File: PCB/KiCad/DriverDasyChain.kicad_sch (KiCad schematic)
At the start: 34 parts, among them J1 Conn_01x02, J10 Conn_01x06, J11 Conn_01x07_Socket, J12 Conn_01x03, J13 Conn_01x03, J16 Conn_01x02, J2 Conn_01x02, J4 Conn_01x04, J5 Conn_01x03, J7 Conn_01x07_Pin, J8 Conn_01x07_Pin, J9 Conn_01x07_Socket, Q2 Q_NMOS_GDS, SW2 SW_DPST_x2, U1 AP2112K-3.3, U2 XIAO-ESP32-S3-DIP, U3 74AHCT1G125, U4 SN65HVD230

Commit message: Keine Änderungen vorgenommen.
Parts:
- removed J1, J2: Conn_01x02, Connector_Molex:Molex_Micro-Fit_3.0_43650-0300_1x03_P3.00mm_Horizontal, symbol Connector_Generic:Conn_01x02
- removed J10: Conn_01x06, Connector_JST:JST_XH_B6B-XH-A_1x06_P2.50mm_Vertical, symbol Connector_Generic:Conn_01x06
- added C11: 100n, symbol Device:C
- added D2: D_Zener, symbol Device:D_Zener
- added J1, J2: Conn_01x03, Connector_Molex:Molex_Micro-Fit_3.0_43650-0300_1x03_P3.00mm_Horizontal, symbol Connector_Generic:Conn_01x03
- added R6: 1M, symbol Device:R
- C10: value 100p -> 1n
- R5: footprint (none) -> Resistor_SMD:R_0603_1608Metric_Pad0.98x0.95mm_HandSolder
- SW2: footprint (none) -> Button_Switch_SMD:SW_DIP_SPSTx01_Slide_6.7x4.1mm_W6.73mm_P2.54mm_LowProfile_JPin
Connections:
- net GPIO A0 (XIAO-ESP32-S3) is gone; now on net GPIO D0 (XIAO-ESP32-S3): J8.7 (Pin_7)
- net GPIO A1 (XIAO-ESP32-S3) is gone; now on an unnamed net: J8.6 (Pin_6)
- net CANH: now also J1.2 (Pin_2), J2.2 (Pin_2)
- net CANL: now also J1.1 (Pin_1), J2.1 (Pin_1)
- net GND: now also C11.1, R6.2
- net Treiber Out: now also R2.1, U3.4
- net at C10.1, J5.2 (Pin_2), Q2.1 (G)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: no longer J7.4 (Pin_4)
- net GPIO D0 (XIAO-ESP32-S3): now reaches R3.1, U3.2
- net GPIO D0 (XIAO-ESP32-S3): no longer J7.5 (Pin_5)
- net GPIO A2 (XIAO-ESP32-S3): no longer names the net of J8.5 (Pin_5)
- net GPIO RX (XIAO-ESP32-S3): no longer names the net of J7.7 (Pin_7)
- net GPIO RX (XIAO-ESP32-S3): no longer U4.4 (R)
- net GPIO TX (XIAO-ESP32-S3): no longer names the net of J8.1 (Pin_1)
- net GPIO TX (XIAO-ESP32-S3): no longer U4.1 (D)
- new net CAN RX: J7.5 (Pin_5), U4.4 (R)
- new net CAN TX: J7.4 (Pin_4), U4.1 (D)
- new net CAN_SHLD: C11.2, J1.3 (Pin_3), J2.3 (Pin_3), R6.1
- no-connect marks 6 -> 9
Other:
- note added: "Daisy Chain Roboterlink"
- note removed: "Extra Output"
- moved on the sheet: C1, C10, C2, C3, C4, C5, C6, C7, C8, C9, D1, J11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

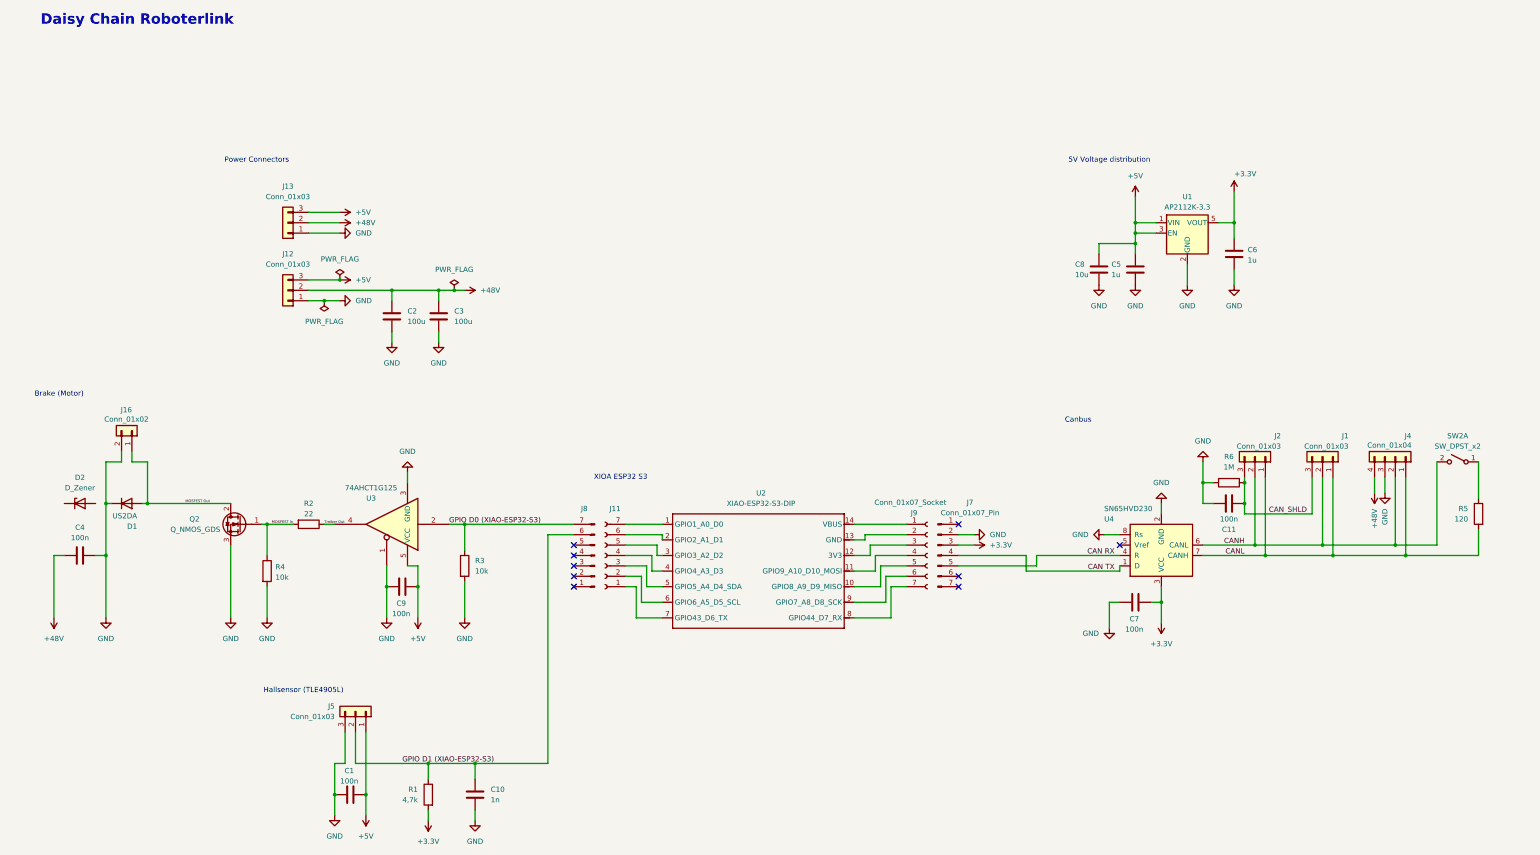
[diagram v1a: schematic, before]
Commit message: Refactor PCB documentation for R0192 Daisy Chain Driverlink-PCB
- Updated the main documentation file `pcb_daisy_chain.md` to enhance clarity and structure, including detailed descriptions of functional blocks, design decisions, and GPIO assignments.
- Removed obsolete references to the MCP2515 and clarified the use of the SN65HVD230 CAN transceiver.
- Added detailed information on the brake control mechanism, including PWM control strategies and safety considerations.
- Introduced a new lock file for KiCad project management.
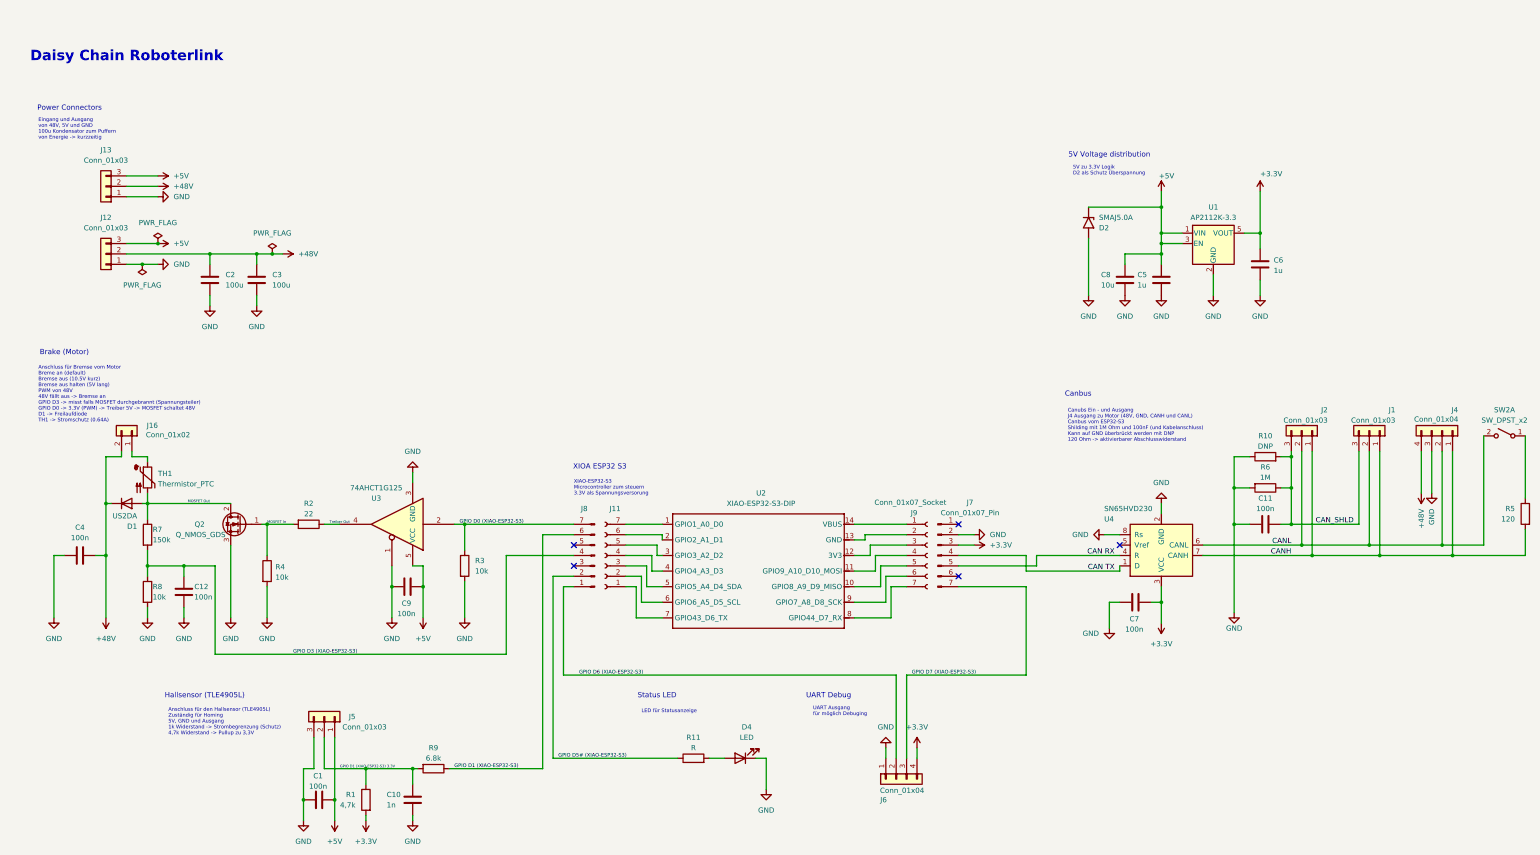
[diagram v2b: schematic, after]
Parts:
- removed D2: D_Zener, symbol Device:D_Zener
- added C12: 100n, symbol Device:C
- added D2: SMAJ5.0A, Diode_SMD:D_SMA, symbol Diode:SMAJ5.0A
- added D4: LED, LED_SMD:LED_0603_1608Metric_Pad1.05x0.95mm_HandSolder, symbol Device:LED
- added J6: Conn_01x04, symbol Connector_Generic:Conn_01x04
- added R10: DNP, symbol Device:R
- added R11: R, symbol Device:R
- added R7: 150k, symbol Device:R
- added R8: 10k, symbol Device:R
- added R9: 6.8k, symbol Device:R
- added TH1: Thermistor_PTC, symbol Device:Thermistor_PTC
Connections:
- net +3.3V: now also J6.4 (Pin_4)
- net +48V: now also C4.2, D1.1 (K), J16.2 (Pin_2); no longer C4.1
- net +5V: now also D2.1 (A1)
- net CANH: now also J1.1 (Pin_1), J2.1 (Pin_1), J4.1 (Pin_1), R5.2, U4.7 (CANH); no longer J1.2 (Pin_2), J2.2 (Pin_2), J4.2 (Pin_2), SW2.2 (B), U4.6 (CANL)
- net CANL: now also J1.2 (Pin_2), J2.2 (Pin_2), J4.2 (Pin_2), SW2.2 (B), U4.6 (CANL); no longer J1.1 (Pin_1), J2.1 (Pin_1), J4.1 (Pin_1), R5.2, U4.7 (CANH)
- net CAN_SHLD: now also R10.2
- net GND: now also C4.1, C12.2, D2.2 (A2), D4.1 (K), J6.1 (Pin_1), R10.1, R8.2; no longer C4.2, D1.1 (K), J16.2 (Pin_2)
- net at C10.1, J5.2 (Pin_2), Q2.1 (G)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: now also R9.2; no longer J8.6 (Pin_6)
- net GPIO D7 (XIAO-ESP32-S3): now reaches J7.7 (Pin_7)
- net GPIO D7 (XIAO-ESP32-S3): now also J6.3 (Pin_3)
- net GPIO D6 (XIAO-ESP32-S3): now reaches J8.1 (Pin_1)
- net GPIO D6 (XIAO-ESP32-S3): now also J6.2 (Pin_2)
- net GPIO D5# (XIAO-ESP32-S3): now reaches J8.2 (Pin_2)
- net GPIO D5# (XIAO-ESP32-S3): now also R11.1
- net GPIO D3 (XIAO-ESP32-S3): now reaches J8.4 (Pin_4)
- net GPIO D3 (XIAO-ESP32-S3): now also C12.1, R7.2, R8.1
- net MOSFEST Out renamed MOSFET Out
- net MOSFET Out: now also R7.1, TH1.2; no longer J16.1 (Pin_1)
- new net: J16.1 (Pin_1), TH1.1
- new net: D4.2 (A), R11.2
- new net GPIO D1 (XIAO-ESP32-S3): J8.6 (Pin_6), R9.1
- no-connect marks 9 -> 5
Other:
- note added: "5V zu 3.3V Logik D2 als Schutz Überspannung"
- note added: "Anschluss für Bremse vom Motor Breme an (default) Bremse aus (10.5V kurz) Bremse aus halten (5V lang) PWM von 48V 48V fällt aus -> Bremse an GPIO D3 -> misst falls MOSFET durchgebrannt (Spannungsteiler) GPIO D0 -> 3.3V (PWM) -> Treiber 5V -> MOSFET schaltet 48V D1 -> Freilaufdiode TH1 -> Stromschutz (0.64A)"
- note added: "Anschluss für den Hallsensor (TLE4905L) Zuständig für Homing 5V, GND und Ausgang 1k Widerstand -> Strombegrenzung (Schutz) 4,7k Widerstand -> Pullup zu 3,3V"
- note added: "Canubs Ein - und Ausgang J4 Ausgang zu Motor (48V, GND, CANH und CANL) Canbus vom ESP32-S3 Shilding mit 1M Ohm und 100nF (und Kabelanschluss) Kann auf GND überbrückt werden mit DNP 120 Ohm -> aktivierbarer Abschlusswiderstand"
- note added: "Eingang und Ausgang von 48V, 5V und GND 100u Kondensator zum Puffern von Energie -> kurzzeitig"
- note added: "LED für Statusanzeige"
- note added: "Status LED"
- note added: "UART Ausgang für möglich Debuging"
- note added: "UART Debug"
- note added: "XIAO-ESP32-S3 Microcontroller zum steuern 3.3V als Spannungsversorung"
- moved on the sheet: C1, C10, C11, C2, C3, C5, C6, C8, C9, J1, J12, J13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

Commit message: Add SN74AHCT1G125 datasheet and update .DS_Store
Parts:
- removed SW2: SW_DPST_x2, Button_Switch_SMD:SW_DIP_SPSTx01_Slide_6.7x4.1mm_W6.73mm_P2.54mm_LowProfile_JPin, symbol Switch:SW_DPST_x2
- added SW1: SW_DPST, Button_Switch_SMD:SW_DIP_SPSTx02_Slide_6.7x6.64mm_W6.73mm_P2.54mm_LowProfile_JPin, symbol Switch:SW_DPST
- C2, C3: Note (none) -> mind. 100V Spannungsfest
- D1: Note (none) -> mind. 100V Variante eher 200V
- J11, J9: Note (none) -> kein Footprint - nur Platzhalter
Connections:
- net CANH: now also SW1.1; no longer R5.2
- net CANL: now also SW1.3
- net at R5.1: now also SW1.4
- new net: R5.2, SW1.2
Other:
- note added: "5V zu 3.3V Logik D2 als Schutz Überspannung Imax = 600mA"
- note added: "Anschluss für Bremse vom Motor Breme an (default) Bremse aus (10.5V kurz) Bremse aus halten (5V lang) PWM von 48V 48V fällt aus -> Bremse an GPIO D3 -> misst falls MOSFET durchgebrannt (Spannungsteiler) Spannungsteiler -> max 5V bei 80V Versorung (können nicht anliegen) C12 -> "lässt" kein PVM durch zur Spannnungsmessung GPIO D0 -> 3.3V (PWM) -> 3.3V Treiber 5V -> 5V MOSFET schaltet 48V D1 -> Fre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"
- note added: "Eingang und Ausgang von 48V, 5V und GND 100u (ca. 100V fest) Kondensator zum Puffern von Energie -> kurzzeitig"
- note added: "XIAO-ESP32-S3 Microcontroller zum steuern 3.3V als Spannungsversorung J9 und J11 nur Platzhalter"
- note removed: "5V zu 3.3V Logik D2 als Schutz Überspannung"
- note removed: "Anschluss für Bremse vom Motor Breme an (default) Bremse aus (10.5V kurz) Bremse aus halten (5V lang) PWM von 48V 48V fällt aus -> Bremse an GPIO D3 -> misst falls MOSFET durchgebrannt (Spannungsteiler) GPIO D0 -> 3.3V (PWM) -> Treiber 5V -> MOSFET schaltet 48V D1 -> Freilaufdiode TH1 -> Stromschutz (0.64A)"
- note removed: "Eingang und Ausgang von 48V, 5V und GND 100u Kondensator zum Puffern von Energie -> kurzzeitig"
- note removed: "XIAO-ESP32-S3 Microcontroller zum steuern 3.3V als Spannungsversorung"
- moved on the sheet: C2, C3, J12, J13, R5

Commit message: Refactor code structure for improved readability and maintainability
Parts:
- C11, C12: footprint (none) -> Capacitor_SMD:C_0603_1608Metric_Pad1.08x0.95mm_HandSolder
- J1, J2: Kabel (none) -> CFBUS.PVC.021 (aufgetrennt); Note (none) -> 1 x Kabel: Aderquerschnitt: 0,5 mm², Außendurchmesser: 2,9 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
- J12: Kabel (none) -> CF77.UL.15.04.D (aufgetrennt); Note (none) -> 1 x Kabel: Aderquerschnitt: 1,5 mm², Außendurchmesser: 2,3 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
- J13: Kabel (none) -> CF77.UL.15.04.D (aufgetrennt); Note (none) -> 1 x Kabel: ca. Aderquerschnitt: 1,5 mm², Außendurchmesser: 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
- J16: footprint Connector_JST:JST_SH_SM02B-SRSS-TB_1x02-1MP_P1.00mm_Horizontal -> Connector_JST:JST_PH_S2B-PH-K_1x02_P2.00mm_Horizontal; Note (none) -> 1 x Kabel: ca. Aderquerschnitt: 0,081 mm², Außendurchmesser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
- J5: Note (none) -> 1 x Kabel: Aderquerschnitt: 0,14 mm², Außendurchmesser: 1,1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
- J6: footprint (none) -> Connector_JST:JST_ZH_B4B-ZR_1x04_P1.50mm_Vertical; Note (none) -> nur Platzhalter -> nicht auflöten
- R10, R11, R6, R7, R8, R9: footprint (none) -> Resistor_SMD:R_0603_1608Metric_Pad0.98x0.95mm_HandSolder

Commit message: Refactor code structure for improved readability and maintainability
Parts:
- J1, J2: footprint Connector_Molex:Molex_Micro-Fit_3.0_43650-0300_1x03_P3.00mm_Horizontal -> TerminalBlock_Phoenix:TerminalBlock_Phoenix_PTSM-0,5-3-2.5-V-THR_1x03_P2.50mm_Vertical
- J12, J13: footprint Connector_AMASS:AMASS_MR30PW-M_1x03_P3.50mm_Horizontal -> TerminalBlock_WAGO:TerminalBlock_WAGO_2601-3104_1x04_P3.50mm_Vertical
- J16: footprint Connector_JST:JST_PH_S2B-PH-K_1x02_P2.00mm_Horizontal -> TerminalBlock_Phoenix:TerminalBlock_Phoenix_PTSM-0,5-2-2,5-V-SMD_1x02-1MP_P2.50mm_Vertical
- J4: footprint R0192:AMASS_XT30PW_2+2-M_1x04_P5.00mm_Horizontal -> TerminalBlock_WAGO:TerminalBlock_WAGO_2601-3104_1x04_P3.50mm_Vertical
- J5: footprint Connector_JST:JST_PH_S3B-PH-K_1x03_P2.00mm_Horizontal -> TerminalBlock_Phoenix:TerminalBlock_Phoenix_PTSM-0,5-3-2.5-V-THR_1x03_P2.50mm_Vertical
- J6: footprint Connector_JST:JST_ZH_B4B-ZR_1x04_P1.50mm_Vertical -> TerminalBlock_Phoenix:TerminalBlock_Phoenix_PTSM-0,5-4-2.5-V-THR_1x04_P2.50mm_Vertical
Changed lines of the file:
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@@
 			)
 		)
-		(property "Footprint" "Connector_JST:JST_ZH_B4B-ZR_1x04_P1.50mm_Vertical"
+		(property "Footprint" "TerminalBlock_Phoenix:TerminalBlock_Phoenix_PTSM-0,5-4-2.5-V-THR_1x04_P2.50mm_Vertical"
 			(at 237.49 218.44 0)
 			(hide yes)
@@
 			)
 		)
-		(property "Footprint" "Connector_JST:JST_PH_S3B-PH-K_1x03_P2.00mm_Horizontal"
+		(property "Footprint" "TerminalBlock_Phoenix:TerminalBlock_Phoenix_PTSM-0,5-3-2.5-V-THR_1x03_P2.50mm_Vertical"
 			(at 97.79 203.2 0)
 			(hide yes)
@@
 			)
 		)
-		(property "Footprint" "Connector_AMASS:AMASS_MR30PW-M_1x03_P3.50mm_Horizontal"
+		(property "Footprint" "TerminalBlock_WAGO:TerminalBlock_WAGO_2601-3104_1x04_P3.50mm_Vertical"
 			(at 198.12 85.09 0)
 			(hide yes)
@@
 			)
 		)
-		(property "Footprint" "R0192:AMASS_XT30PW_2+2-M_1x04_P5.00mm_Horizontal"
+		(property "Footprint" "TerminalBlock_WAGO:TerminalBlock_WAGO_2601-3104_1x04_P3.50mm_Vertical"
 			(at 370.84 133.35 0)
 			(hide yes)
@@
 			)
 		)
-		(property "Footprint" "Connector_Molex:Molex_Micro-Fit_3.0_43650-0300_1x03_P3.00mm_Horizontal"
+		(property "Footprint" "TerminalBlock_Phoenix:TerminalBlock_Phoenix_PTSM-0,5-3-2.5-V-THR_1x03_P2.50mm_Vertical"
 			(at 353.06 133.35 0)
 			(hide yes)
@@
 			)
 		)
-		(property "Footprint" "Connector_AMASS:AMASS_MR30PW-M_1x03_P3.50mm_Horizontal"
+		(property "Footprint" "TerminalBlock_WAGO:TerminalBlock_WAGO_2601-3104_1x04_P3.50mm_Vertical"
 			(at 198.12 101.6 0)
 			(hide yes)
@@
 			)
 		)
-		(property "Footprint" "Connector_Molex:Molex_Micro-Fit_3.0_43650-0300_1x03_P3.00mm_Horizontal"
+		(property "Footprint" "TerminalBlock_Phoenix:TerminalBlock_Phoenix_PTSM-0,5-3-2.5-V-THR_1x03_P2.50mm_Vertical"
 			(at 336.55 133.35 0)
 			(hide yes)
@@
 			)
 		)
-		(property "Footprint" "Connector_JST:JST_PH_S2B-PH-K_1x02_P2.00mm_Horizontal"
+		(property "Footprint" "TerminalBlock_Phoenix:TerminalBlock_Phoenix_PTSM-0,5-2-2,5-V-SMD_1x02-1MP_P2.50mm_Vertical"
 			(at 50.8 133.35 0)
 			(hide yes)
